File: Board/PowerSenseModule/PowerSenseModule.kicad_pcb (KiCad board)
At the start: 2 copper layers, 91.1 x 62.3 mm, 71 parts, among them J1 DT13-6P, J3 Programming Header, J4 Board Interconnect, U1 TPS82150, U2 NCV2007x, U3 dsPIC33EV32GM102, U4 MCP2542FDxMF, Y1 25 MHz

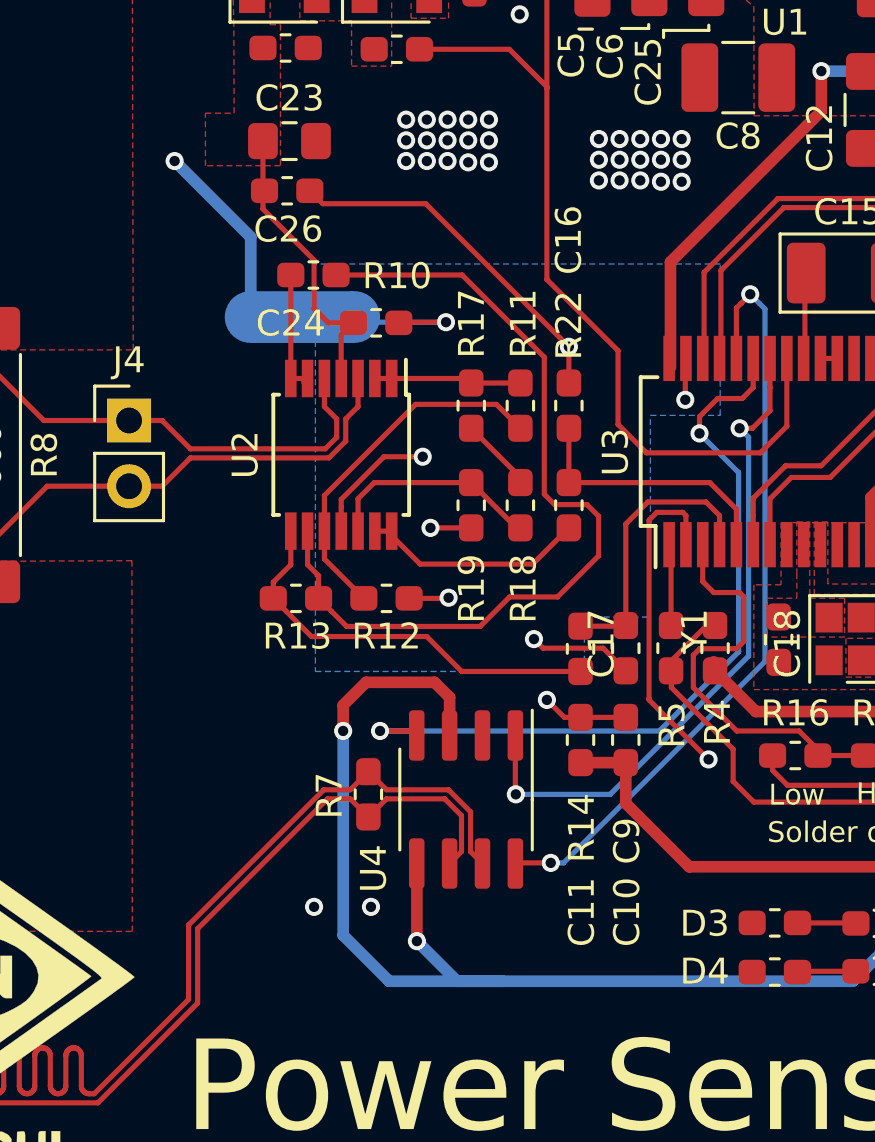
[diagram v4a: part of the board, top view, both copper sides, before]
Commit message: Moved op amp decoupling cap closer to Vdd
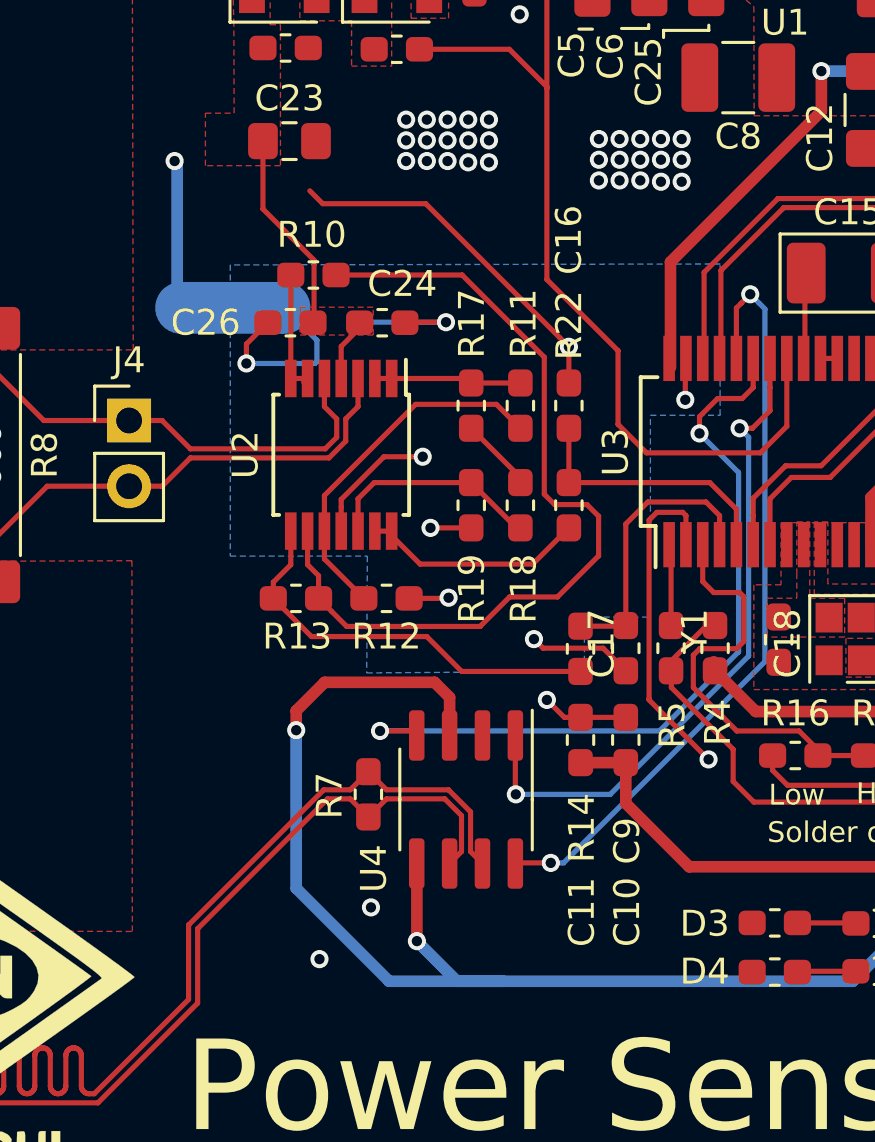
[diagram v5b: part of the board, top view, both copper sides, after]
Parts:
- moved C26 5.10 mm to (159.7, 86.8), turned to 180 degrees
- moved NT1 2.71 mm to (157.5, 86.2)
- moved C24 0.24 mm to (163.2, 86.8)
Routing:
- net GNDA: track 33.2 -> 40.5 mm, vias 7 -> 8
- net +5V: track 186.0 -> 188.4 mm
- net GND: track 42.3 -> 40.5 mm
- net VS: track 11.4 -> 10.3 mm

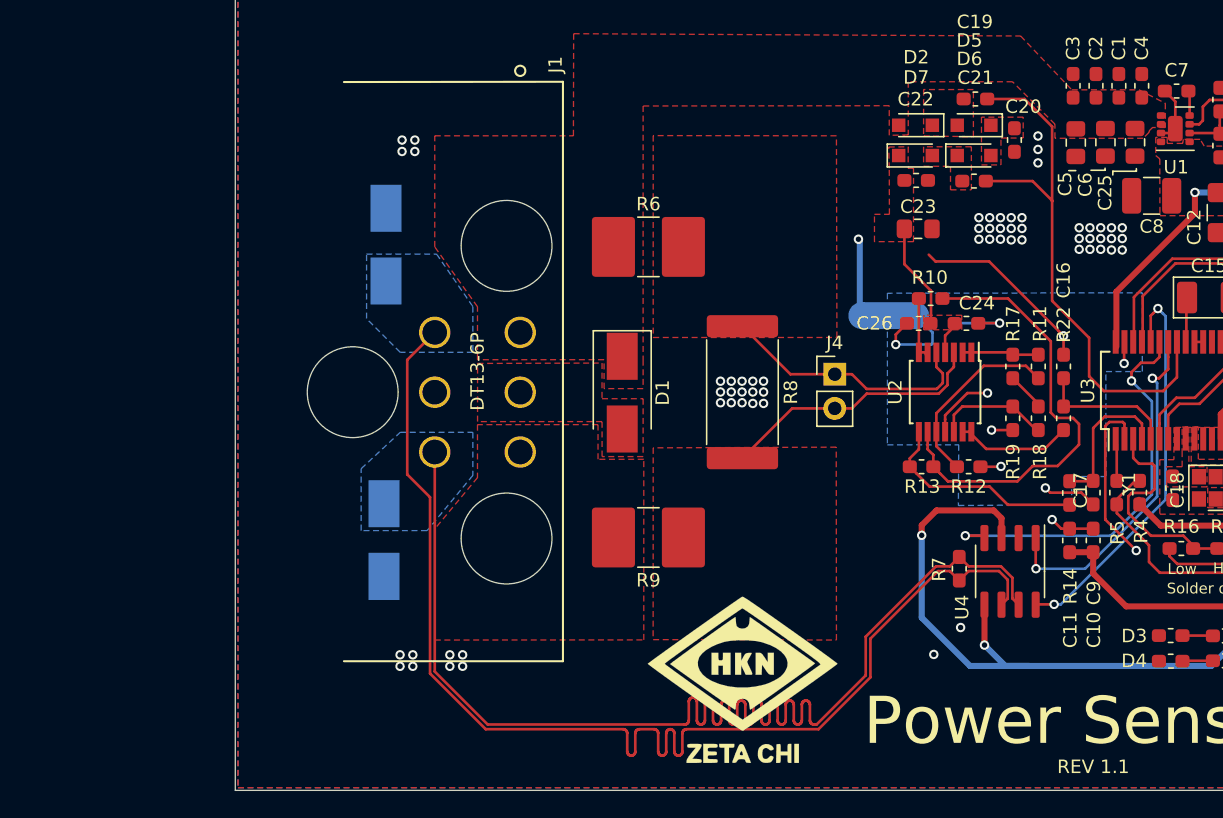
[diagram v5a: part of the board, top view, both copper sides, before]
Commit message: schematic changes and PCB adjustments
- had V2 and V1 reversed for differential amplifier so that was fixed by flipping U2C so that the non-inverting input was connected to (through a buffer) to SENSE+. The resistors and connections were adjusted to make the flip work.
- changed hole size of the DT13-6P connector- they were correct in the first place (3mm not 5mm)
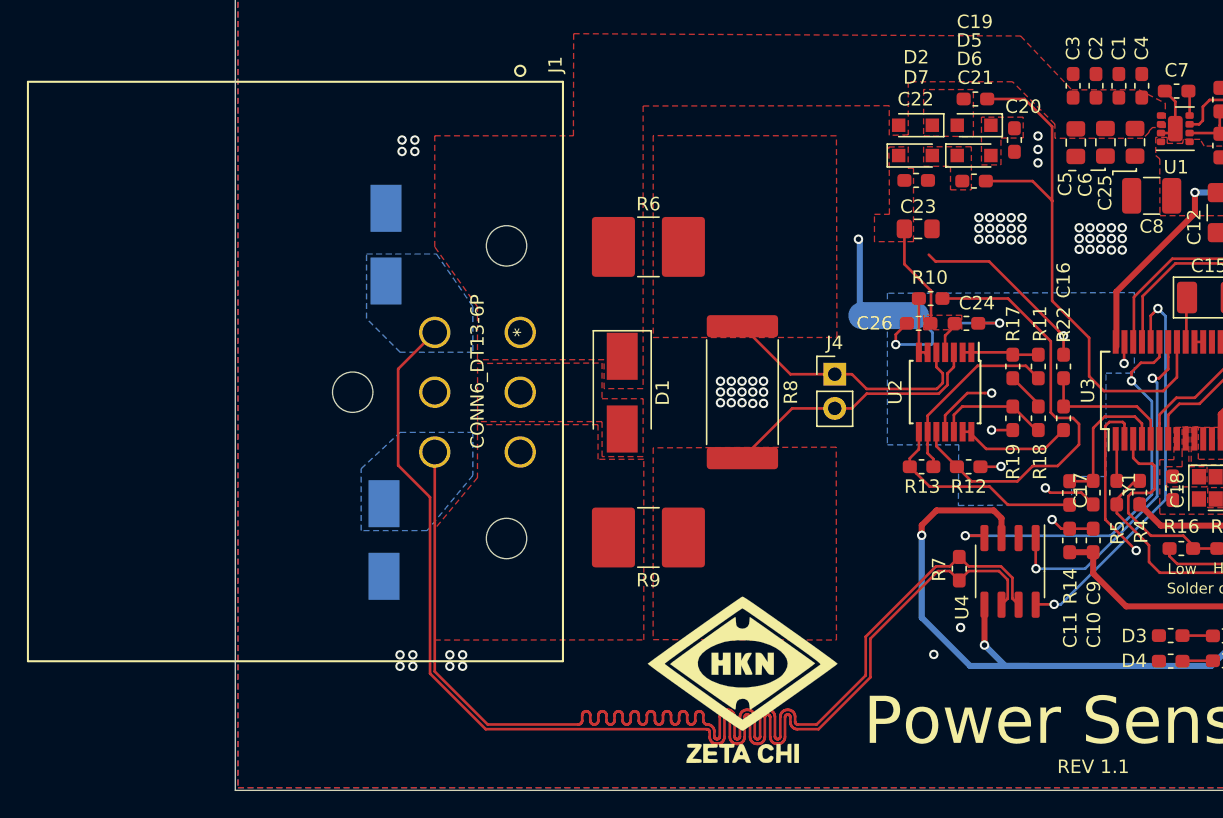
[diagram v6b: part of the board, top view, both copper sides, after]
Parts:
- J1: value DT13-6P -> CONN6_DT13-6P
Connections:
- R12 pad 1: Net-(R11-Pad1) -> Net-(R10-Pad1)
- R13 pad 2: Net-(R10-Pad1) -> Net-(R11-Pad1)
- U2 pad 10: Net-(R11-Pad1) -> Net-(R10-Pad1)
- U2 pad 9: Net-(R10-Pad1) -> Net-(R11-Pad1)
- Y1 pad 2: (no net) -> Net-(Y1-Pad2)
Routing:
- net /CAN-: track 91.2 -> 96.2 mm
- net /CAN+: track 95.3 -> 96.8 mm
- net Net-(R10-Pad1): track 33.8 -> 32.5 mm

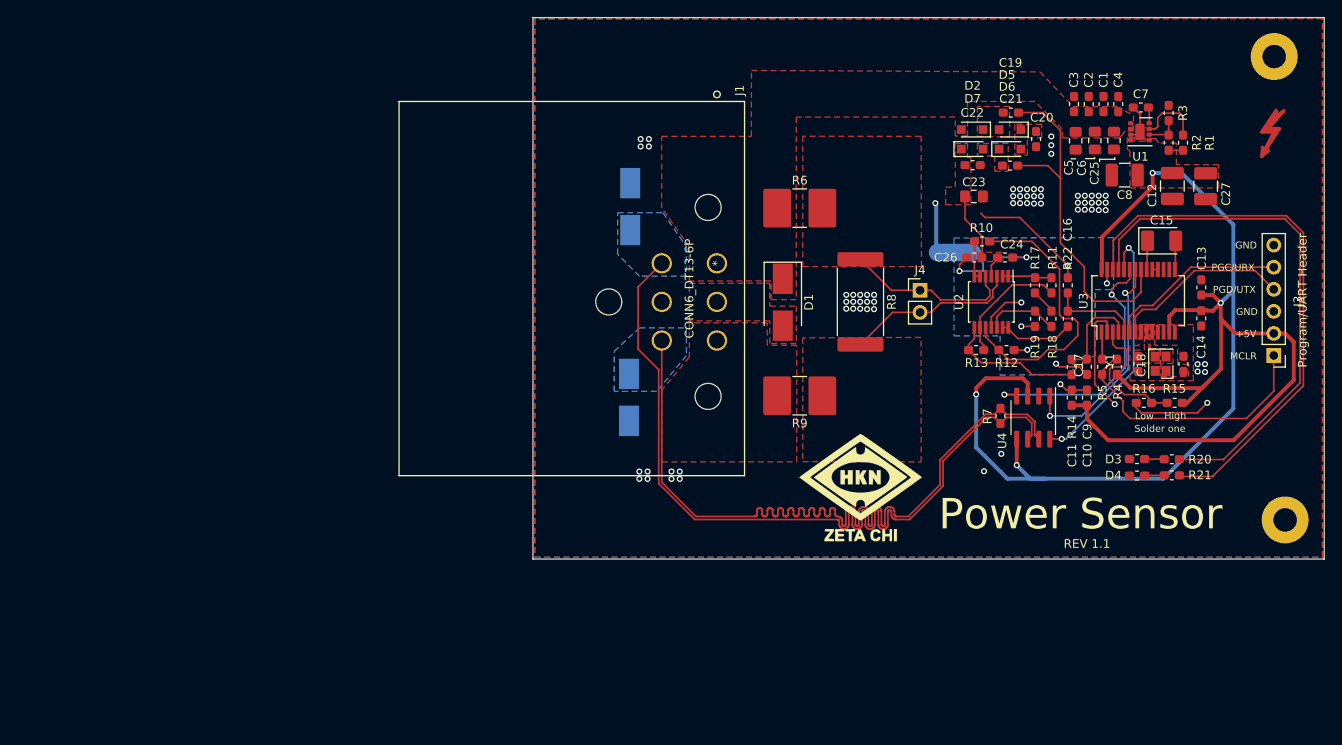
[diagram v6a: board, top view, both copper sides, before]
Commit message: Added drawings dimensions, changed footprint of op amp, and cleaned up
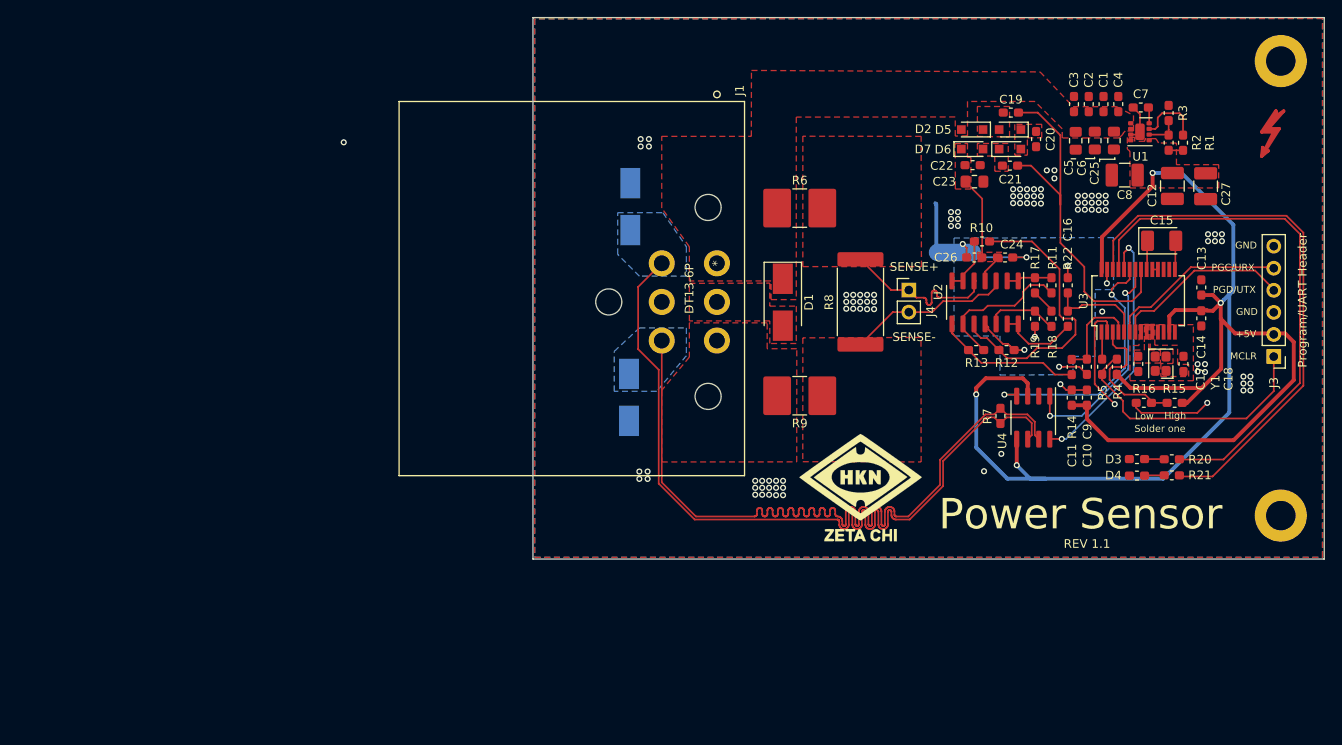
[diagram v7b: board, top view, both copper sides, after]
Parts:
- J1: value CONN6_DT13-6P -> DT13-6P
- U2: footprint Package_SO:TSSOP-14_4.4x5mm_P0.65mm -> Package_SO:SOIC-14_3.9x8.7mm_P1.27mm
- moved C23 1.71 mm to (159.7, 78.0)
- moved J4 1.29 mm to (152.2, 90.5)
- moved H1 0.92 mm to (195.0, 64.2)
- moved U2 0.72 mm to (160.9, 91.9)
- moved H2 0.71 mm to (195.0, 116.5)
- moved J3 0.12 mm to (194.2, 98.2)
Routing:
- net GNDA: track 40.8 -> 25.2 mm, vias 8 -> 7
- net Net-(R11-Pad1): track 14.1 -> 17.3 mm
- net VS: track 10.3 -> 12.8 mm
- net /PWM: track 41.1 -> 42.7 mm
- net Net-(R10-Pad2): track 4.86 -> 6.36 mm
- net /MCU and CAN/VSENSE: track 10.4 -> 11.4 mm
- net Net-(R13-Pad1): track 15.9 -> 16.8 mm
- net Net-(R10-Pad1): track 32.5 -> 33.3 mm
- net Net-(R22-Pad2): track 8.64 -> 9.37 mm
- net GND: vias 70 -> 99
- net (no net): vias 0 -> 1
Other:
- board text added: "1.9mm"
- board text added: "1mm"
- board text added: "2X"
- board text added: "3.4mm, M3 screw"
- board text added: "3X"
- board text added: "3mm, M2.5 screw"
- board text added: "6X"
- board text added: "SENSE+"
- board text added: "SENSE-"
- board text added: "See DT13-6P drawings for hole spacings"

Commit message: Changed Dt13 footprint to be shorter and regen gerber
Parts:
- J1: value DT13-6P -> CONN6_DT13-6P
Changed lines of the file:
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@@
     (diff_pair_gap 0.15)
+  )
+  (module Connector_TE:DT13-6P (layer F.Cu)
+    (at 130.08 87.44 90)
+    (fp_text reference J1 (at 19.89 2.62 90) (layer F.SilkS)
+      (effects (font (size 1 1) (thickness 0.15)))
+    )
+    (fp_text value CONN6_DT13-6P (at -2.9083 -3.175 90) (layer F.SilkS)
+      (effects (font (size 1 1) (thickness 0.15)))
+    )
+    (fp_circle (center 19.431 0) (end 19.812 0) (layer B.SilkS) (width 0.1524))
+    (fp_circle (center 19.431 0) (end 19.812 0) (layer F.SilkS) (width 0.1524))
+    (fp_circle (center 0 2.54) (end 0.381 2.54) (layer F.Fab) (width 0.1524))
+    (fp_line (start 18.4912 -36.449) (end -24.3078 -36.449) (layer F.CrtYd) (width 0.1524))
+    (fp_line (start 18.4912 3.048) (end 18.4912 -36.449) (layer F.CrtYd) (width 0.1524))
+    (fp_line (start -24.3078 3.048) (end 18.4912 3.048) (layer F.CrtYd) (width 0.1524))
+    (fp_line (start -24.3078 -36.449) (end -24.3078 3.048) (layer F.CrtYd) (width 0.1524))
+    (fp_line (start 18.7452 -36.703) (end -24.5618 -36.703) (layer F.CrtYd) (width 0.1524))
+    (fp_line (start 18.7452 3.302) (end 18.7452 -36.703) (layer F.CrtYd) (width 0.1524))
+    (fp_line (start -24.5618 3.302) (end 18.7452 3.302) (layer F.CrtYd) (width 0.1524))
+    (fp_line (start -24.5618 -36.703) (end -24.5618 3.302) (layer F.CrtYd) (width 0.1524))
+    (fp_line (start -24.3078 -36.449) (end -24.3078 3.048) (layer F.Fab) (width 0.1524))
+    (fp_line (start 18.4912 -36.449) (end -24.3078 -36.449) (layer F.Fab) (width 0.1524))
+    (fp_line (start 18.4912 3.048) (end 18.4912 -36.449) (layer F.Fab) (width 0.1524))
+    (fp_line (start -24.3078 3.048) (end 18.4912 3.048) (layer F.Fab) (width 0.1524))
+    (fp_line (start -24.4348 -16) (end -24.4348 3.175) (layer F.SilkS) (width 0.1524))
+    (fp_line (start 18.6182 3.175) (end 18.6182 -16) (layer F.SilkS) (width 0.1524))
+    (fp_line (start -24.4348 3.175) (end 18.6182 3.175) (layer F.SilkS) (width 0.1524))
+    (fp_text user * (at 0 0 90) (layer F.SilkS)
+      (effects (font (size 1 1) (thickness 0.15)))
+    )
+    (fp_text user J1 (at 20.37 0.98 90) (layer Dwgs.User)
+      (effects (font (size 1 1) (thickness 0.15)))
+    )
+    (fp_text user DT13-6P (at 22.97 2.48 90) (layer Dwgs.User)
+      (effects (font (size 1 1) (thickness 0.15)))
+    )
+    (pad "" np_thru_hole circle (at -4.445 -12.446 90) (size 3 3) (drill 3) (layers *.Cu *.Mask))
+    (pad "" np_thru_hole circle (at 6.4262 -1.016 90) (size 3 3) (drill 3) (layers *.Cu *.Mask))
+    (pad "" np_thru_hole circle (at -15.3162 -1.016 90) (size 3 3) (drill 3) (layers *.Cu *.Mask))
+    (pad 3 thru_hole circle (at -8.89 0 90) (size 3 3) (drill 1.8288) (layers *.Cu *.Mask)
+      (net 18 /MEAS_OUT))
+    (pad 4 thru_hole circle (at -8.89 -6.35 90) (size 3 3) (drill 1.8288) (layers *.Cu *.Mask)
+      (net 37 /CAN+))
+    (pad 2 thru_hole circle (at -4.445 0 90) (size 3 3) (drill 1.8288) (layers *.Cu *.Mask)
+      (net 1 GND))
+    (pad 5 thru_hole circle (at -4.445 -6.35 90) (size 3 3) (drill 1.8288) (layers *.Cu *.Mask)
+      (net 1 GND))
+    (pad 1 thru_hole circle (at 0 0 90) (size 3 3) (drill 1.8288) (layers *.Cu *.Mask)
+      (net 2 +12V))
+    (pad 6 thru_hole circle (at 0 -6.35 90) (size 3 3) (drill 1.8288) (layers *.Cu *.Mask)
+      (net 38 /CAN-))
   )
   (module Package_SO:SOIC-14_3.9x8.7mm_P1.27mm (layer F.Cu)
@@
       (net 1 GND))
   )
-  (module Connector_TE:DT13-6P (layer F.Cu)
-    (at 130.08 87.44 90)
-    (fp_text reference J1 (at 19.89 2.62 90) (layer F.SilkS)
-      (effects (font (size 1 1) (thickness 0.15)))
-    )
-    (fp_text value DT13-6P (at -2.9083 -3.175 90) (layer F.SilkS)
-      (effects (font (size 1 1) (thickness 0.15)))
-    )
-    (fp_circle (center 19.431 0) (end 19.812 0) (layer B.SilkS) (width 0.1524))
-    (fp_circle (center 19.431 0) (end 19.812 0) (layer F.SilkS) (width 0.1524))
-    (fp_circle (center 0 2.54) (end 0.381 2.54) (layer F.Fab) (width 0.1524))
-    (fp_line (start 18.4912 -36.449) (end -24.3078 -36.449) (layer F.CrtYd) (width 0.1524))
-    (fp_line (start 18.4912 3.048) (end 18.4912 -36.449) (layer F.CrtYd) (width 0.1524))
-    (fp_line (start -24.3078 3.048) (end 18.4912 3.048) (layer F.CrtYd) (width 0.1524))
-    (fp_line (start -24.3078 -36.449) (end -24.3078 3.048) (layer F.CrtYd) (width 0.1524))
-    (fp_line (start 18.7452 -36.703) (end -24.5618 -36.703) (layer F.CrtYd) (width 0.1524))
-    (fp_line (start 18.7452 3.302) (end 18.7452 -36.703) (layer F.CrtYd) (width 0.1524))
-    (fp_line (start -24.5618 3.302) (end 18.7452 3.302) (layer F.CrtYd) (width 0.1524))
-    (fp_line (start -24.5618 -36.703) (end -24.5618 3.302) (layer F.CrtYd) (width 0.1524))
-    (fp_line (start -24.3078 -36.449) (end -24.3078 3.048) (layer F.Fab) (width 0.1524))
-    (fp_line (start 18.4912 -36.449) (end -24.3078 -36.449) (layer F.Fab) (width 0.1524))
-    (fp_line (start 18.4912 3.048) (end 18.4912 -36.449) (layer F.Fab) (width 0.1524))
-    (fp_line (start -24.3078 3.048) (end 18.4912 3.048) (layer F.Fab) (width 0.1524))
-    (fp_line (start -24.4348 -36.576) (end -24.4348 3.175) (layer F.SilkS) (width 0.1524))
-    (fp_line (start 18.6182 -36.576) (end -24.4348 -36.576) (layer F.SilkS) (width 0.1524))
-    (fp_line (start 18.6182 3.175) (end 18.6182 -36.576) (layer F.SilkS) (width 0.1524))
-    (fp_line (start -24.4348 3.175) (end 18.6182 3.175) (layer F.SilkS) (width 0.1524))
-    (fp_text user * (at 0 0 90) (layer F.SilkS)
-      (effects (font (size 1 1) (thickness 0.15)))
-    )
-    (fp_text user J1 (at 20.37 0.98 90) (layer Dwgs.User)
-      (effects (font (size 1 1) (thickness 0.15)))
-    )
-    (fp_text user DT13-6P (at 22.97 2.48 90) (layer Dwgs.User)
-      (effects (font (size 1 1) (thickness 0.15)))
-    )
-    (pad "" np_thru_hole circle (at -4.445 -12.446 90) (size 3 3) (drill 3) (layers *.Cu *.Mask Dwgs.User))
-    (pad "" np_thru_hole circle (at 6.4262 -1.016 90) (size 3 3) (drill 3) (layers *.Cu *.Mask Dwgs.User))
-    (pad "" np_thru_hole circle (at -15.3162 -1.016 90) (size 3 3) (drill 3) (layers *.Cu *.Mask Dwgs.User))
-    (pad 3 thru_hole circle (at -8.89 0 90) (size 3 3) (drill 1.8288) (layers *.Cu *.Mask Dwgs.User)
-      (net 18 /MEAS_OUT))
-    (pad 4 thru_hole circle (at -8.89 -6.35 90) (size 3 3) (drill 1.8288) (layers *.Cu *.Mask Dwgs.User)
-      (net 37 /CAN+))
-    (pad 2 thru_hole circle (at -4.445 0 90) (size 3 3) (drill 1.8288) (layers *.Cu *.Mask Dwgs.User)
-      (net 1 GND))
-    (pad 5 thru_hole circle (at -4.445 -6.35 90) (size 3 3) (drill 1.8288) (layers *.Cu *.Mask Dwgs.User)
-      (net 1 GND))
-    (pad 1 thru_hole circle (at 0 0 90) (size 3 3) (drill 1.8288) (layers *.Cu *.Mask Dwgs.User)
-      (net 2 +12V))
-    (pad 6 thru_hole circle (at 0 -6.35 90) (size 3 3) (drill 1.8288) (layers *.Cu *.Mask Dwgs.User)
-      (net 38 /CAN-))
-  )
   (module Symbol:Symbol_Highvoltage_Type1_CopperTop_Small (layer F.Cu)
